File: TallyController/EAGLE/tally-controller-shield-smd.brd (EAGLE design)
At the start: 101.6 x 53.3 mm, 42 parts, among them J2 Mega R3, SW1 B3U-1000P, U1 SN75174N, U2 SN75174N, U3 SN75174N

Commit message: Add decoupling caps to shield.
Remove non-SMD version of shield (no-longer being worked on).
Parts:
- added C2, C3, C4, C5, C6, C7: (no value), Nordic_nRF:RESC0805_N
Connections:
- net GND: now also C2.2, C3.2, C4.2, C5.2, C6.2, C7.2
- net VCC: now also C2.1, C3.1, C4.1, C5.1, C6.1, C7.1
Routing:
- net VCC: track 159.6 -> 176.3 mm
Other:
- board text added: "ATEM Tally Controller Rev 1.4"
- board text removed: "ATEM Tally Controller Rev 1.3"
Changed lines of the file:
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@@
 <drawing>
 <settings>
-<setting alwaysvectorfont="no"/>
+<setting alwaysvectorfont="yes"/>
 <setting verticaltext="up"/>
 </settings>
@@
 <layer number="115" name="ReferenceISLANDS" color="7" fill="1" visible="yes" active="yes"/>
 <layer number="116" name="Patch_BOT" color="9" fill="4" visible="yes" active="yes"/>
+<layer number="117" name="BACKMAAT1" color="7" fill="1" visible="yes" active="yes"/>
 <layer number="118" name="Rect_Pads" color="7" fill="1" visible="yes" active="yes"/>
+<layer number="119" name="KAP_TEKEN" color="7" fill="1" visible="yes" active="yes"/>
+<layer number="120" name="KAP_MAAT1" color="7" fill="1" visible="yes" active="yes"/>
 <layer number="121" name="_tsilk" color="7" fill="1" visible="yes" active="yes"/>
 <layer number="122" name="_bsilk" color="7" fill="1" visible="yes" active="yes"/>
@@
 <layer number="128" name="_bValues" color="7" fill="1" visible="yes" active="yes"/>
 <layer number="129" name="Mask" color="7" fill="1" visible="yes" active="yes"/>
+<layer number="130" name="SMDSTROOK" color="7" fill="1" visible="yes" active="yes"/>
 <layer number="131" name="tAdjust" color="7" fill="1" visible="no" active="yes"/>
 <layer number="132" name="bAdjust" color="7" fill="1" visible="no" active="yes"/>
+<layer number="133" name="bottom_silk" color="7" fill="1" visible="yes" active="yes"/>
 <layer number="144" name="Drill_legend" color="7" fill="1" visible="yes" active="yes"/>
 <layer number="150" name="Notes" color="7" fill="1" visible="no" active="yes"/>
@@
 <layer number="230" name="230bmp" color="7" fill="1" visible="yes" active="yes"/>
 <layer number="231" name="231bmp" color="7" fill="1" visible="yes" active="yes"/>
+<layer number="232" name="Eagle3D_PG2" color="7" fill="1" visible="yes" active="yes"/>
+<layer number="233" name="Eagle3D_PG3" color="7" fill="1" visible="yes" active="yes"/>
 <layer number="248" name="Housing" color="7" fill="1" visible="yes" active="yes"/>
 <layer number="249" name="Edge" color="7" fill="1" visible="yes" active="yes"/>
@@
 <text x="2.3368" y="10.3124" size="1.778" layer="25" align="top-left">ATEM Tally
 Controller
-Rev 1.3</text>
+Rev 1.4</text>
 <text x="43.815" y="6.35" size="0.6096" layer="25" ratio="15" align="center-left">5V</text>
 <text x="52.705" y="6.35" size="0.6096" layer="25" ratio="15" align="center-left">5V</text>
@@
 <attribute name="VALUE" x="17.62" y="-0.36" size="1.27" layer="27"/>
 </element>
+<element name="C2" library="Nordic_nRF" library_urn="urn:adsk.eagle:library:169009" package="RESC0805_N" package3d_urn="urn:adsk.eagle:package:2593736/1" value="" x="40.64" y="42.545" smashed="yes" rot="MR270">
+<attribute name="NAME" x="39.14" y="43.545" size="1.27" layer="26" rot="MR270"/>
+<attribute name="VALUE" x="43.14" y="43.545" size="1.27" layer="28" rot="MR270"/>
+</element>
+<element name="C3" library="Nordic_nRF" library_urn="urn:adsk.eagle:library:169009" package="RESC0805_N" package3d_urn="urn:adsk.eagle:package:2593736/1" value="" x="71.12" y="42.545" smashed="yes" rot="MR270">
+<attribute name="NAME" x="69.62" y="43.545" size="1.27" layer="26" rot="MR270"/>
+<attribute name="VALUE" x="73.62" y="43.545" size="1.27" layer="28" rot="MR270"/>
+</element>
+<element name="C4" library="Nordic_nRF" library_urn="urn:adsk.eagle:library:169009" package="RESC0805_N" package3d_urn="urn:adsk.eagle:package:2593736/1" value="" x="71.12" y="23.495" smashed="yes" rot="MR270">
+<attribute name="NAME" x="69.62" y="24.495" size="1.27" layer="26" rot="MR270"/>
+<attribute name="VALUE" x="73.62" y="24.495" size="1.27" layer="28" rot="MR270"/>
+</element>
+<element name="C5" library="Nordic_nRF" library_urn="urn:adsk.eagle:library:169009" package="RESC0805_N" package3d_urn="urn:adsk.eagle:package:2593736/1" value="" x="8.89" y="46.355" smashed="yes" rot="MR0">
+<attribute name="NAME" x="9.89" y="47.855" size="1.27" layer="26" rot="MR0"/>
+<attribute name="VALUE" x="9.89" y="43.855" size="1.27" layer="28" rot="MR0"/>
+</element>
+<element name="C6" library="Nordic_nRF" library_urn="urn:adsk.eagle:library:169009" package="RESC0805_N" package3d_urn="urn:adsk.eagle:package:2593736/1" value="" x="24.13" y="46.355" smashed="yes" rot="MR0">
+<attribute name="NAME" x="25.13" y="47.855" size="1.27" layer="26" rot="MR0"/>
+<attribute name="VALUE" x="25.13" y="43.855" size="1.27" layer="28" rot="MR0"/>
+</element>
+<element name="C7" library="Nordic_nRF" library_urn="urn:adsk.eagle:library:169009" package="RESC0805_N" package3d_urn="urn:adsk.eagle:package:2593736/1" value="" x="31.75" y="6.985" smashed="yes" rot="MR0">
+<attribute name="NAME" x="32.75" y="8.485" size="1.27" layer="26" rot="MR0"/>
+<attribute name="VALUE" x="32.75" y="4.485" size="1.27" layer="28" rot="MR0"/>
+</element>
 </elements>
 <signals>
@@
 <vertex x="-2.54" y="13.335"/>
 </polygon>
+<contactref element="C2" pad="2"/>
+<contactref element="C3" pad="2"/>
+<contactref element="C4" pad="2"/>
+<contactref element="C5" pad="2"/>
+<contactref element="C6" pad="2"/>
+<contactref element="C7" pad="2"/>
+<via x="74.93" y="29.21" extent="1-16" drill="0.35"/>
 </signal>
 <signal name="MEGASDA">
@@
 <contactref element="J2" pad="8"/>
 <contactref element="U1" pad="1"/>
-<wire x1="40.64" y1="38.1" x2="40.64" y2="43.18" width="0.1524" layer="16"/>
-<wire x1="40.64" y1="43.18" x2="41.91" y2="44.45" width="0.1524" layer="16"/>
-<wire x1="41.91" y1="44.45" x2="41.91" y2="50.546" width="0.1524" layer="16"/>
+<wire x1="40.64" y1="38.1" x2="40.64" y2="38.735" width="0.1524" layer="16"/>
+<wire x1="40.64" y1="38.735" x2="41.91" y2="40.005" width="0.1524" layer="16"/>
+<wire x1="41.91" y1="40.005" x2="41.91" y2="50.546" width="0.1524" layer="16"/>
 <wire x1="41.91" y1="50.546" x2="41.656" y2="50.8" width="0.1524" layer="16"/>
 </signal>
@@
 <wire x1="52.07" y1="24.09" x2="52.07" y2="25.4" width="1.016" layer="16"/>
 <wire x1="52.07" y1="25.4" x2="53.34" y2="26.67" width="1.016" layer="16"/>
-<wire x1="40.64" y1="45.72" x2="38.1" y2="43.18" width="1.016" layer="16"/>
+<wire x1="40.64" y1="45.72" x2="39.37" y2="45.72" width="1.016" layer="16"/>
 <wire x1="35.56" y1="29.21" x2="38.1" y2="26.67" width="1.016" layer="16"/>
-<wire x1="38.1" y1="43.18" x2="38.1" y2="36.83" width="1.016" layer="16"/>
-<wire x1="38.1" y1="36.83" x2="35.56" y2="34.29" width="1.016" layer="16"/>
 <wire x1="35.56" y1="34.29" x2="35.56" y2="29.21" width="1.016" layer="16"/>
 <wire x1="33.655" y1="36.195" x2="35.56" y2="34.29" width="1.016" layer="16"/>
@@
 <wire x1="10.16" y1="38.735" x2="12.7" y2="36.195" width="1.016" layer="16"/>
 <wire x1="10.16" y1="43.18" x2="10.16" y2="38.735" width="1.016" layer="16"/>
+<contactref element="C2" pad="1"/>
+<contactref element="C4" pad="1"/>
+<contactref element="C3" pad="1"/>
+<wire x1="40.64" y1="45.72" x2="40.64" y2="43.645" width="0.508" layer="16"/>
+<wire x1="71.12" y1="45.72" x2="71.12" y2="43.645" width="0.508" layer="16"/>
+<wire x1="71.12" y1="26.67" x2="71.12" y2="24.595" width="0.508" layer="16"/>
+<contactref element="C5" pad="1"/>
+<contactref element="C6" pad="1"/>
+<contactref element="C7" pad="1"/>
+<wire x1="33.02" y1="10.16" x2="33.02" y2="7.155" width="0.508" layer="16"/>
+<wire x1="33.02" y1="7.155" x2="32.85" y2="6.985" width="0.508" layer="16"/>
+<wire x1="10.16" y1="43.18" x2="9.99" y2="43.35" width="0.508" layer="16"/>
+<wire x1="9.99" y1="43.35" x2="9.99" y2="46.355" width="0.508" layer="16"/>
+<wire x1="25.4" y1="43.18" x2="25.23" y2="43.35" width="0.508" layer="16"/>
+<wire x1="25.23" y1="43.35" x2="25.23" y2="46.355" width="0.508" layer="16"/>
+<wire x1="39.37" y1="45.72" x2="38.1" y2="44.45" width="1.016" layer="16"/>
+<wire x1="38.1" y1="36.83" x2="35.56" y2="34.29" width="1.016" layer="16"/>
+<wire x1="38.1" y1="44.45" x2="38.1" y2="36.83" width="1.016" layer="16"/>
 </signal>
 <signal name="CAM1DA">

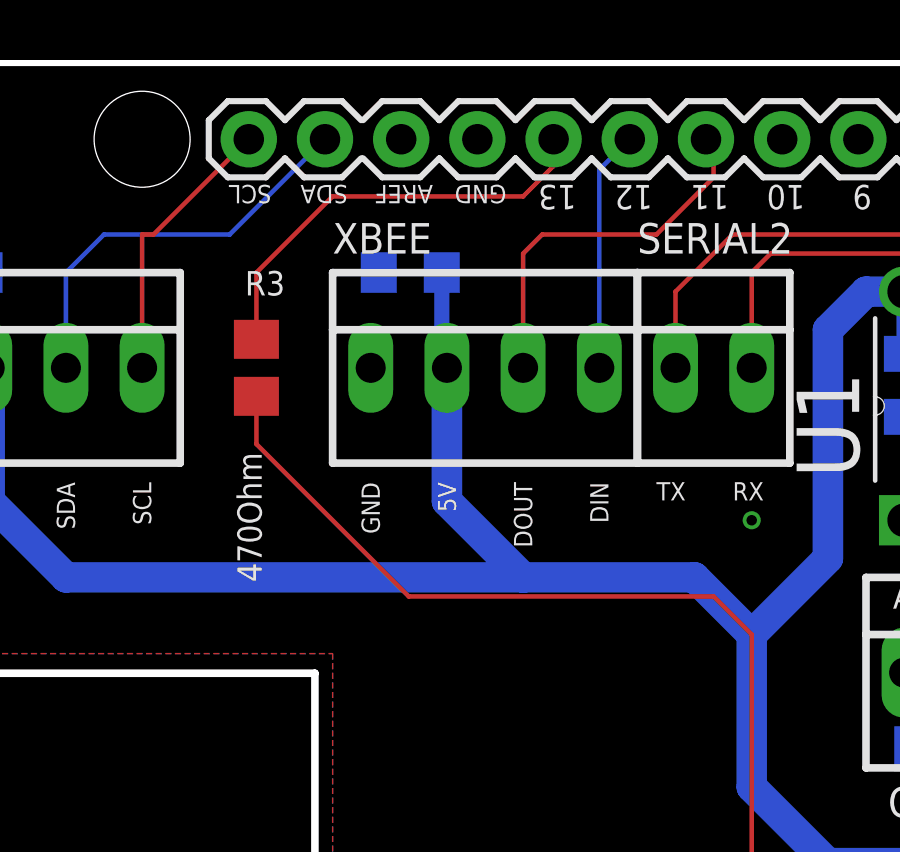
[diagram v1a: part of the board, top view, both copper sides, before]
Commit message: Add optional AREF jumper.  Remove unused nets.
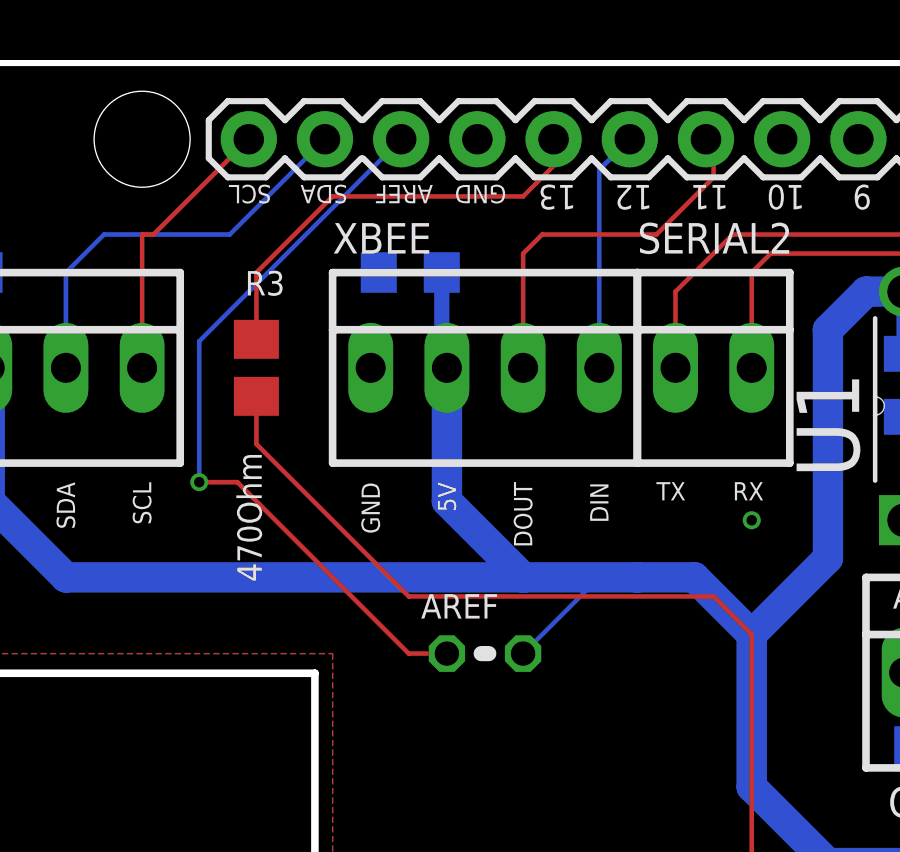
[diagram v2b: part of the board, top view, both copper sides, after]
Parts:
- added AREF: 0ohm, BeagleBone_Black_Wireless:0204V
- C2, C3, C4, C5, C6, C7: value (none) -> 1uf
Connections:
- removed net 5V@1: J2.5V@1
- removed net 5V@2: J2.5V@2
- removed net IOREF: J2.IOREF
- removed net MEGA10: J2.10
- removed net MEGA2: J2.2
- removed net MEGA23: J2.23
- removed net MEGA25: J2.25
- removed net MEGA27: J2.27
- removed net MEGA29: J2.29
- removed net MEGA3: J2.3
- removed net MEGA30: J2.30
- removed net MEGA31: J2.31
- removed net MEGA32: J2.32
- removed net MEGA33: J2.33
- removed net MEGA34: J2.34
- removed net MEGA35: J2.35
- removed net MEGA36: J2.36
- removed net MEGA37: J2.37
- removed net MEGA39: J2.39
- removed net MEGA4: J2.4
- removed net MEGA41: J2.41
- removed net MEGA43: J2.43
- removed net MEGA45: J2.45
- removed net MEGA46: J2.46
- removed net MEGA47: J2.47
- removed net MEGA48: J2.48
- removed net MEGA49: J2.49
- removed net MEGA53: J2.53
- removed net MEGA9: J2.9
- removed net MEGAA10: J2.A10
- removed net MEGAA11: J2.A11
- removed net MEGAA12: J2.A12
- removed net MEGAA13: J2.A13
- removed net MEGAA14: J2.A14
- removed net MEGAA15: J2.A15
- removed net MEGAA3: J2.A3
- removed net MEGAA4: J2.A4
- removed net MEGAA5: J2.A5
- removed net MEGAA6: J2.A6
- removed net MEGAA7: J2.A7
- removed net MEGAA8: J2.A8
- removed net MEGAA9: J2.A9
- removed net MEGAMISO: J2.50
- removed net MEGAMOSI: J2.51
- removed net MEGARX0: J2.0
- removed net MEGARX3: J2.15
- removed net MEGASCL: J2.21
- removed net MEGASCLK: J2.52
- removed net MEGASDA: J2.20
- removed net MEGATX0: J2.1
- removed net MEGATX3: J2.14
- removed net VIN: J2.VIN
- new net AREF: AREF.1, J2.AREF
- net VCC: now also AREF.2
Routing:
- net AREF: track 0.00 -> 24.8 mm, vias 0 -> 1
- net VCC: track 176.3 -> 181.2 mm
